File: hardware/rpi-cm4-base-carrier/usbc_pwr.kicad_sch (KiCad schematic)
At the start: 19 parts, among them J3 USB4105-GF-A, Q1 STL6P3LLH6, U3 STUSB4500QTR

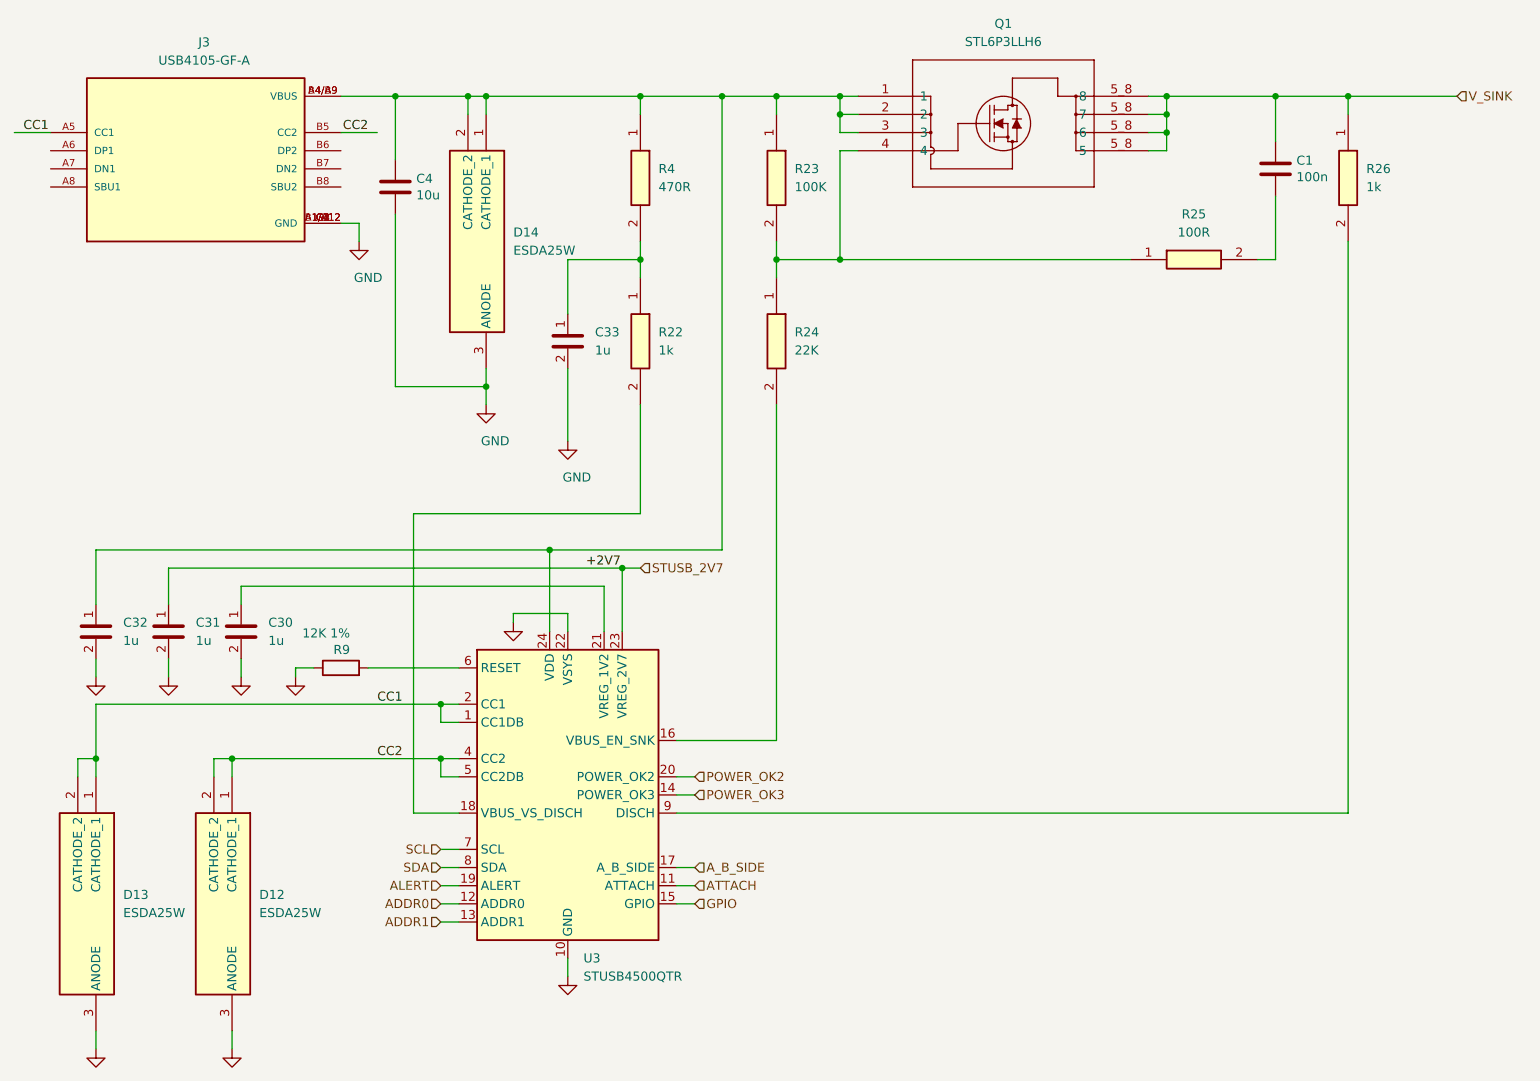
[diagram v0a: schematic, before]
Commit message: PWR regs complete, EMI protection? LDO low noise passthrough??
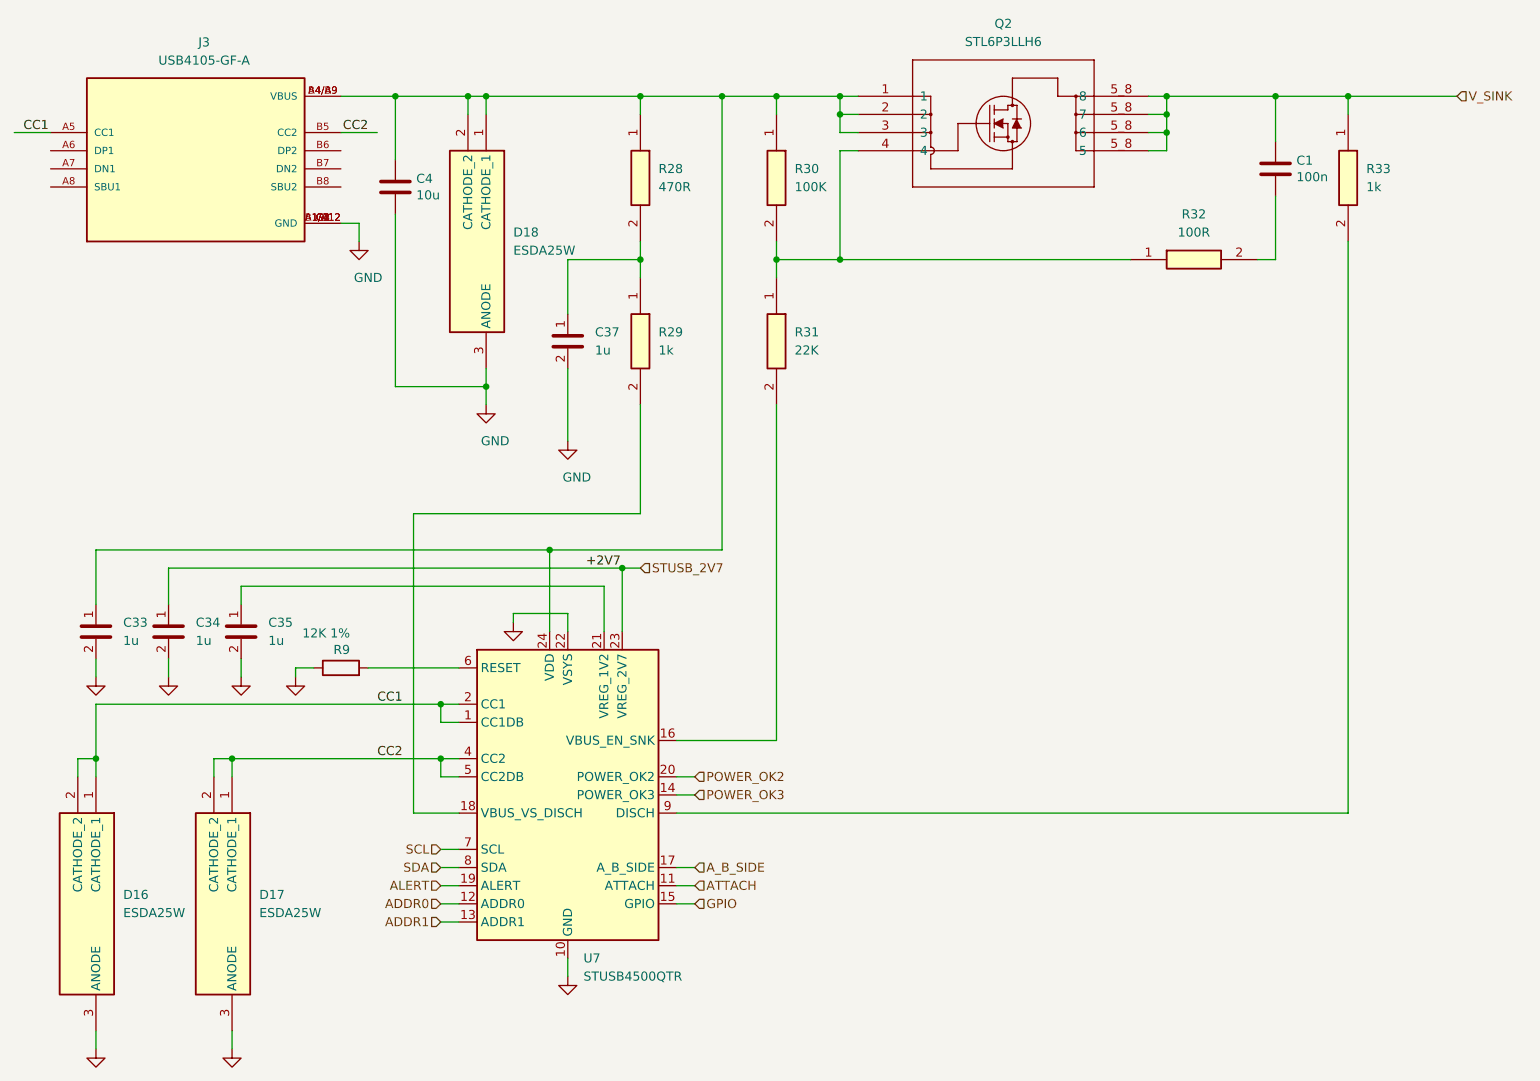
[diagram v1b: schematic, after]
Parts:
- renumbered C32 to C33, C31 to C34, C30 to C35, C33 to C37, D13 to D16, D12 to D17, D14 to D18, Q1 to Q2, R4 to R28, R22 to R29, R23 to R30, R24 to R31, R25 to R32, R26 to R33, U3 to U7
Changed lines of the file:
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@@
   (symbol (lib_id "08055C105JAT2A:08055C105JAT2A") (at 44.45 99.06 270) (unit 1)
     (in_bom yes) (on_board yes) (dnp no) (fields_autoplaced)
-    (property "Reference" "C30" (at 48.26 101.6 90)
+    (property "Reference" "C35" (at 48.26 101.6 90)
       (effects (font (size 1.27 1.27)) (justify left))
     )
@@
   (symbol (lib_id "ESDA25W:ESDA25W") (at 78.74 30.48 270) (unit 1)
     (in_bom yes) (on_board yes) (dnp no) (fields_autoplaced)
-    (property "Reference" "D14" (at 82.55 46.99 90)
+    (property "Reference" "D18" (at 82.55 46.99 90)
       (effects (font (size 1.27 1.27)) (justify left))
     )
@@
   (symbol (lib_id "ESDA25W:ESDA25W") (at 43.18 123.19 270) (unit 1)
     (in_bom yes) (on_board yes) (dnp no) (fields_autoplaced)
-    (property "Reference" "D12" (at 46.99 139.7 90)
+    (property "Reference" "D17" (at 46.99 139.7 90)
       (effects (font (size 1.27 1.27)) (justify left))
     )
@@
   (symbol (lib_id "08055C105JAT2A:08055C105JAT2A") (at 90.17 58.42 270) (unit 1)
     (in_bom yes) (on_board yes) (dnp no) (fields_autoplaced)
-    (property "Reference" "C33" (at 93.98 60.96 90)
+    (property "Reference" "C37" (at 93.98 60.96 90)
       (effects (font (size 1.27 1.27)) (justify left))
     )
@@
   (symbol (lib_id "STL6P3LLH6:STL6P3LLH6") (at 130.81 27.94 0) (unit 1)
     (in_bom yes) (on_board yes) (dnp no) (fields_autoplaced)
-    (property "Reference" "Q1" (at 151.13 17.78 0)
+    (property "Reference" "Q2" (at 151.13 17.78 0)
       (effects (font (size 1.27 1.27)))
     )
@@
   (symbol (lib_id "ESDA25W:ESDA25W") (at 24.13 123.19 270) (unit 1)
     (in_bom yes) (on_board yes) (dnp no) (fields_autoplaced)
-    (property "Reference" "D13" (at 27.94 139.7 90)
+    (property "Reference" "D16" (at 27.94 139.7 90)
       (effects (font (size 1.27 1.27)) (justify left))
     )
@@
   (symbol (lib_id "08055C105JAT2A:08055C105JAT2A") (at 34.29 99.06 270) (unit 1)
     (in_bom yes) (on_board yes) (dnp no) (fields_autoplaced)
-    (property "Reference" "C31" (at 38.1 101.6 90)
+    (property "Reference" "C34" (at 38.1 101.6 90)
       (effects (font (size 1.27 1.27)) (justify left))
     )
@@
   (symbol (lib_id "SamacSys_Parts:CR0402-FX-2202GLF") (at 119.38 53.34 270) (unit 1)
     (in_bom yes) (on_board yes) (dnp no) (fields_autoplaced)
-    (property "Reference" "R24" (at 121.92 60.96 90)
+    (property "Reference" "R31" (at 121.92 60.96 90)
       (effects (font (size 1.27 1.27)) (justify left))
     )
@@
   (symbol (lib_id "SamacSys_Parts:CR0402-FX-1003GLF") (at 119.38 30.48 270) (unit 1)
     (in_bom yes) (on_board yes) (dnp no) (fields_autoplaced)
-    (property "Reference" "R23" (at 121.92 38.1 90)
+    (property "Reference" "R30" (at 121.92 38.1 90)
       (effects (font (size 1.27 1.27)) (justify left))
     )
@@
   (symbol (lib_id "SamacSys_Parts:CR0402AFX-1001GLF") (at 100.33 53.34 270) (unit 1)
     (in_bom yes) (on_board yes) (dnp no) (fields_autoplaced)
-    (property "Reference" "R22" (at 102.87 60.96 90)
+    (property "Reference" "R29" (at 102.87 60.96 90)
       (effects (font (size 1.27 1.27)) (justify left))
     )
@@
   (symbol (lib_id "SamacSys_Parts:CR0402-JW-471GLF") (at 100.33 30.48 270) (unit 1)
     (in_bom yes) (on_board yes) (dnp no) (fields_autoplaced)
-    (property "Reference" "R4" (at 102.87 38.1 90)
+    (property "Reference" "R28" (at 102.87 38.1 90)
       (effects (font (size 1.27 1.27)) (justify left))
     )
@@
   (symbol (lib_id "SamacSys_Parts:CR0402AFX-1001GLF") (at 199.39 30.48 270) (unit 1)
     (in_bom yes) (on_board yes) (dnp no) (fields_autoplaced)
-    (property "Reference" "R26" (at 201.93 38.1 90)
+    (property "Reference" "R33" (at 201.93 38.1 90)
       (effects (font (size 1.27 1.27)) (justify left))
     )
@@
   (symbol (lib_id "08055C105JAT2A:08055C105JAT2A") (at 24.13 99.06 270) (unit 1)
     (in_bom yes) (on_board yes) (dnp no) (fields_autoplaced)
-    (property "Reference" "C32" (at 27.94 101.6 90)
+    (property "Reference" "C33" (at 27.94 101.6 90)
       (effects (font (size 1.27 1.27)) (justify left))
     )
@@
   (symbol (lib_id "Interface_USB:STUSB4500QTR") (at 90.17 125.73 0) (unit 1)
     (in_bom yes) (on_board yes) (dnp no) (fields_autoplaced)
-    (property "Reference" "U3" (at 92.3641 148.59 0)
+    (property "Reference" "U7" (at 92.3641 148.59 0)
       (effects (font (size 1.27 1.27)) (justify left))
     )
@@
   (symbol (lib_id "SamacSys_Parts:CR0402-FX-1000GLF") (at 168.91 50.8 0) (unit 1)
     (in_bom yes) (on_board yes) (dnp no) (fields_autoplaced)
-    (property "Reference" "R25" (at 177.8 44.45 0)
+    (property "Reference" "R32" (at 177.8 44.45 0)
       (effects (font (size 1.27 1.27)))
     )

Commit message: convert IC refs to U refs and re-annotate, add fiducials and extra via stitching to layout
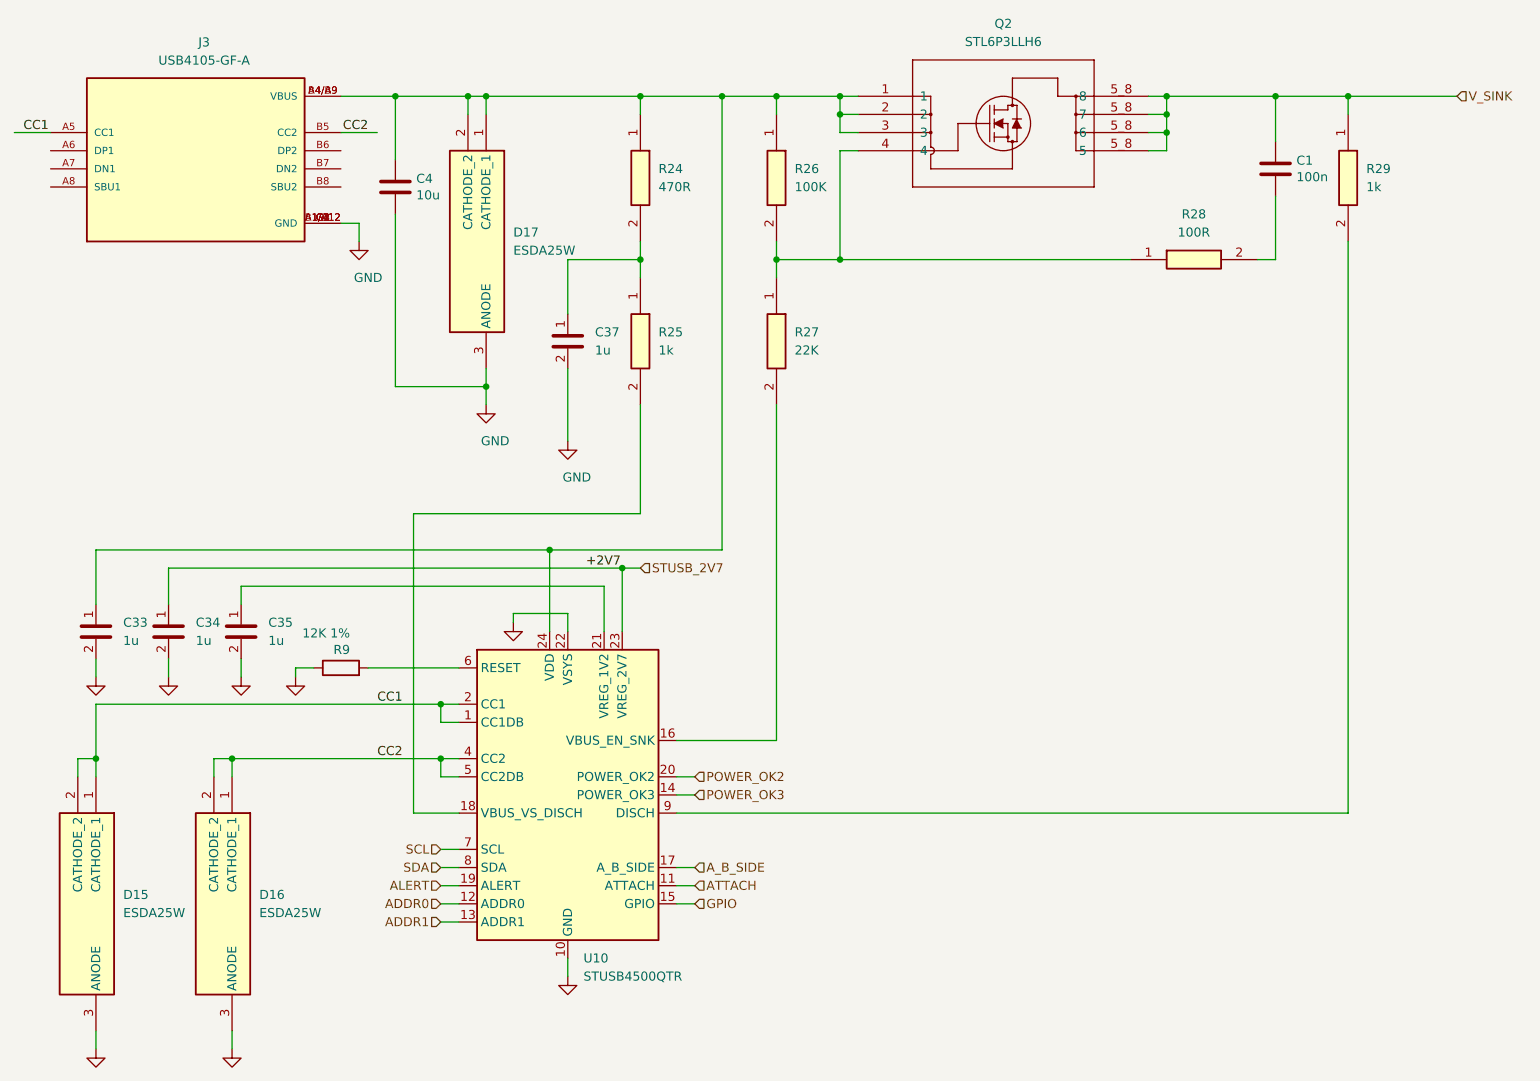
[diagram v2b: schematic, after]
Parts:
- renumbered D16 to D15, D17 to D16, D18 to D17, R28 to R24, R29 to R25, R30 to R26, R31 to R27, R32 to R28, R33 to R29, U7 to U10
